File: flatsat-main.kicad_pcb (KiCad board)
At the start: 4 copper layers, 120 x 150 mm, 26 parts

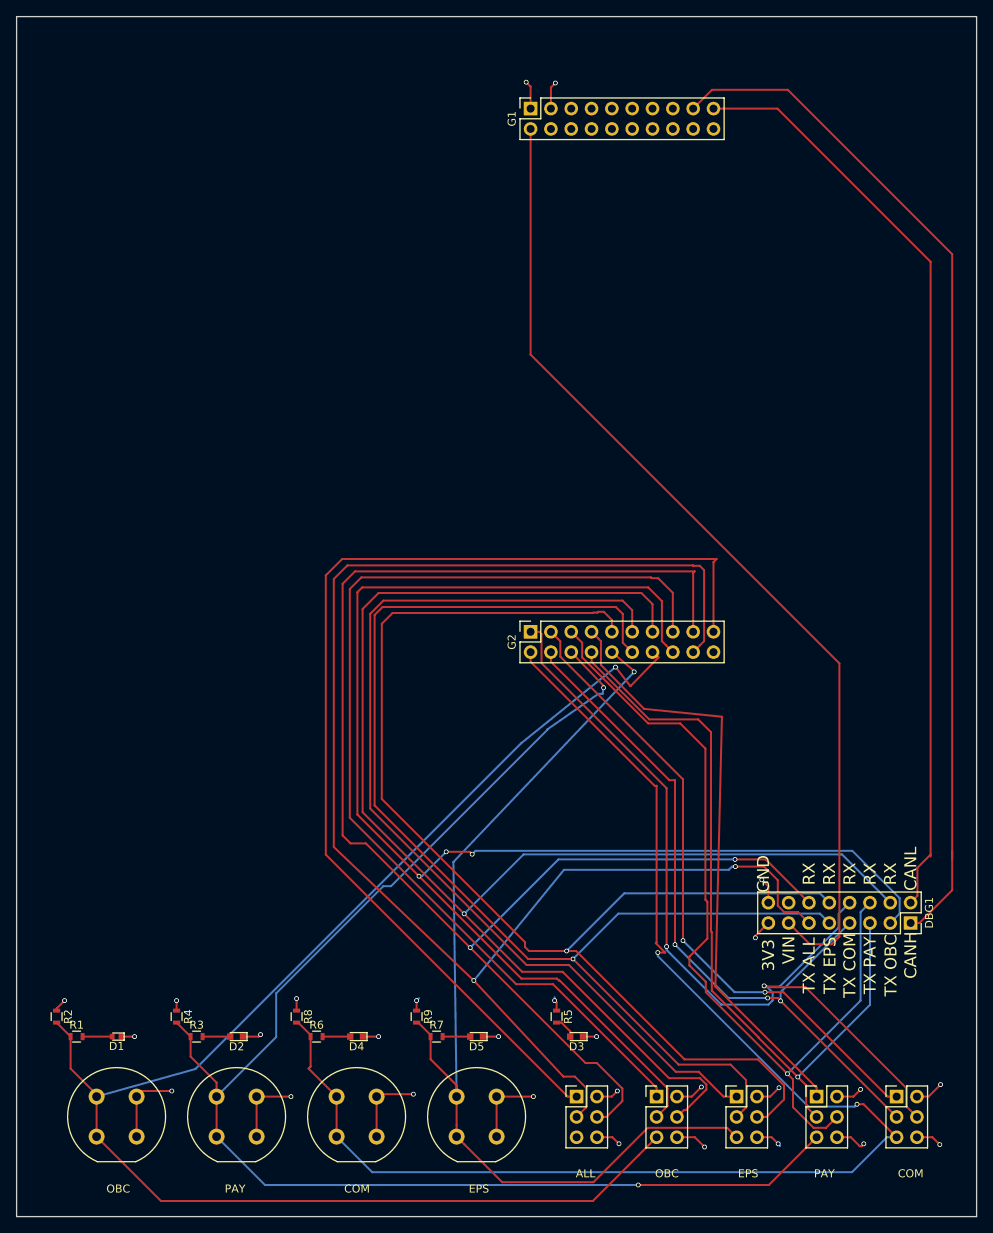
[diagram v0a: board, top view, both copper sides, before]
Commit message: Modified outputs for manufacture.
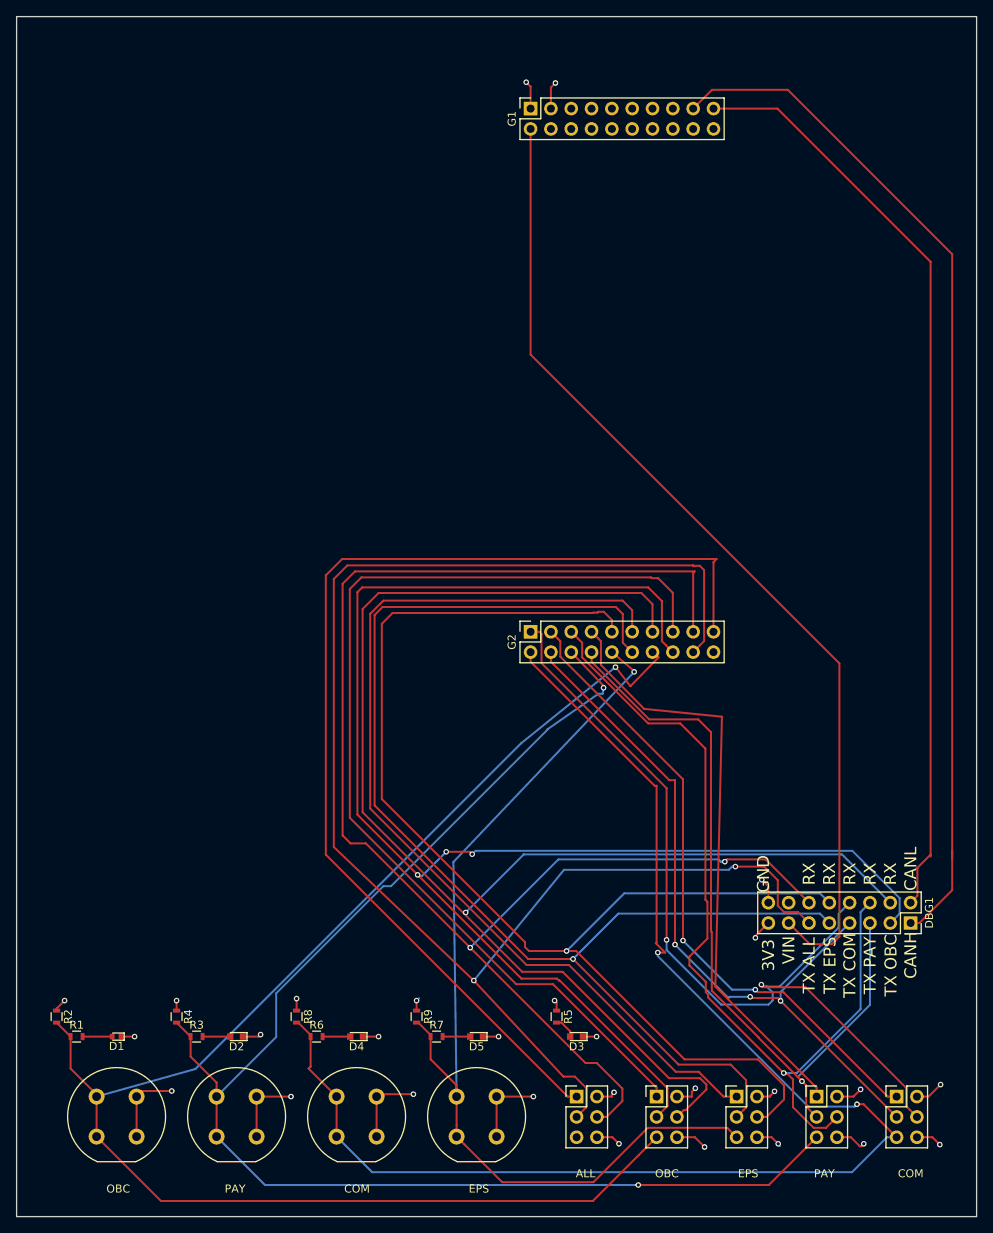
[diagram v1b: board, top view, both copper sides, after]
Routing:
- net /3V3CRIT: track 30.6 -> 28.7 mm
- net /PAY_MOSI_A: track 107.9 -> 109.2 mm
- net /PAY_SCK_A: track 96.3 -> 97.1 mm
- net /COM_MOSI_A: track 109.4 -> 110.0 mm
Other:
- net class Default: via_dia 0.6 -> 0.7
